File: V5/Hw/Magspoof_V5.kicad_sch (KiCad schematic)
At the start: 35 parts, among them J2 SWD, P1 USB_C_Plug_USB2.0, Q1 DMG3415U-7, SW1 ON, SW3 S1, SW4 SOURCE MAG, SW5 RESET, U1 CH552G, U2 AP2112K-3.3, U3 TC4424, U5 MCP73831

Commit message: feat(hw): components got reorganized
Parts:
- H1, H2, H3, H4: footprint MountingHole:MountingHole_2.2mm_M2 -> MountingHole:MountingHole_2.2mm_M2_DIN965_Pad

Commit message: feat(hw): TX and RX pins updated
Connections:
- net RXD: now also U1.8 (P3.0); no longer U1.4 (P1.6)
- net TXD: now also U1.7 (P3.1); no longer U1.5 (P1.7)
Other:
- moved on the sheet: C1, C2, U1

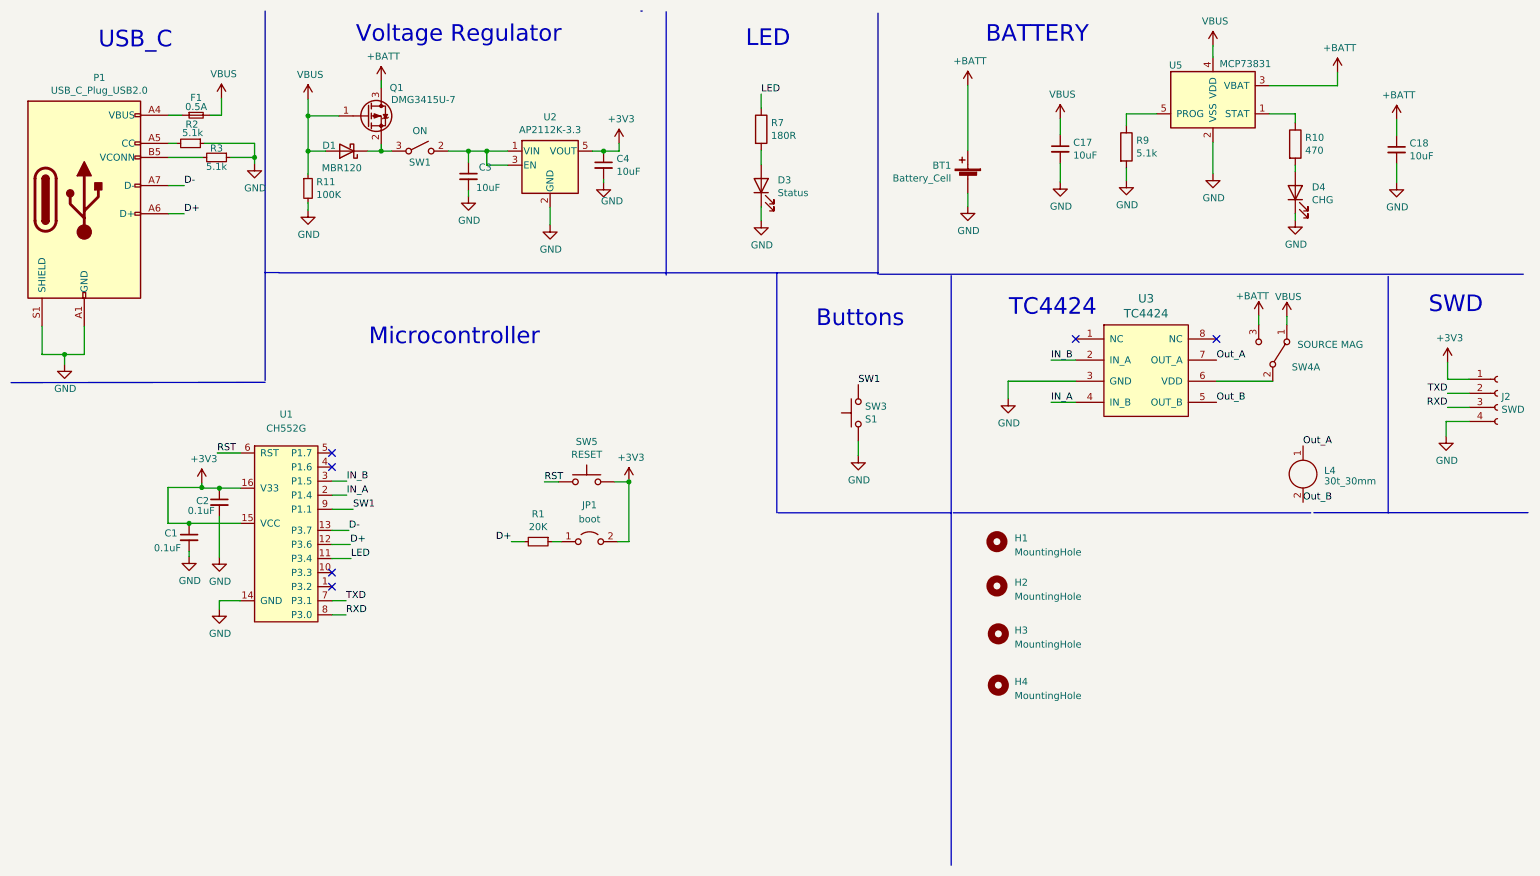
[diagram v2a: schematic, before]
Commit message: fix(hw): pins Serial boot
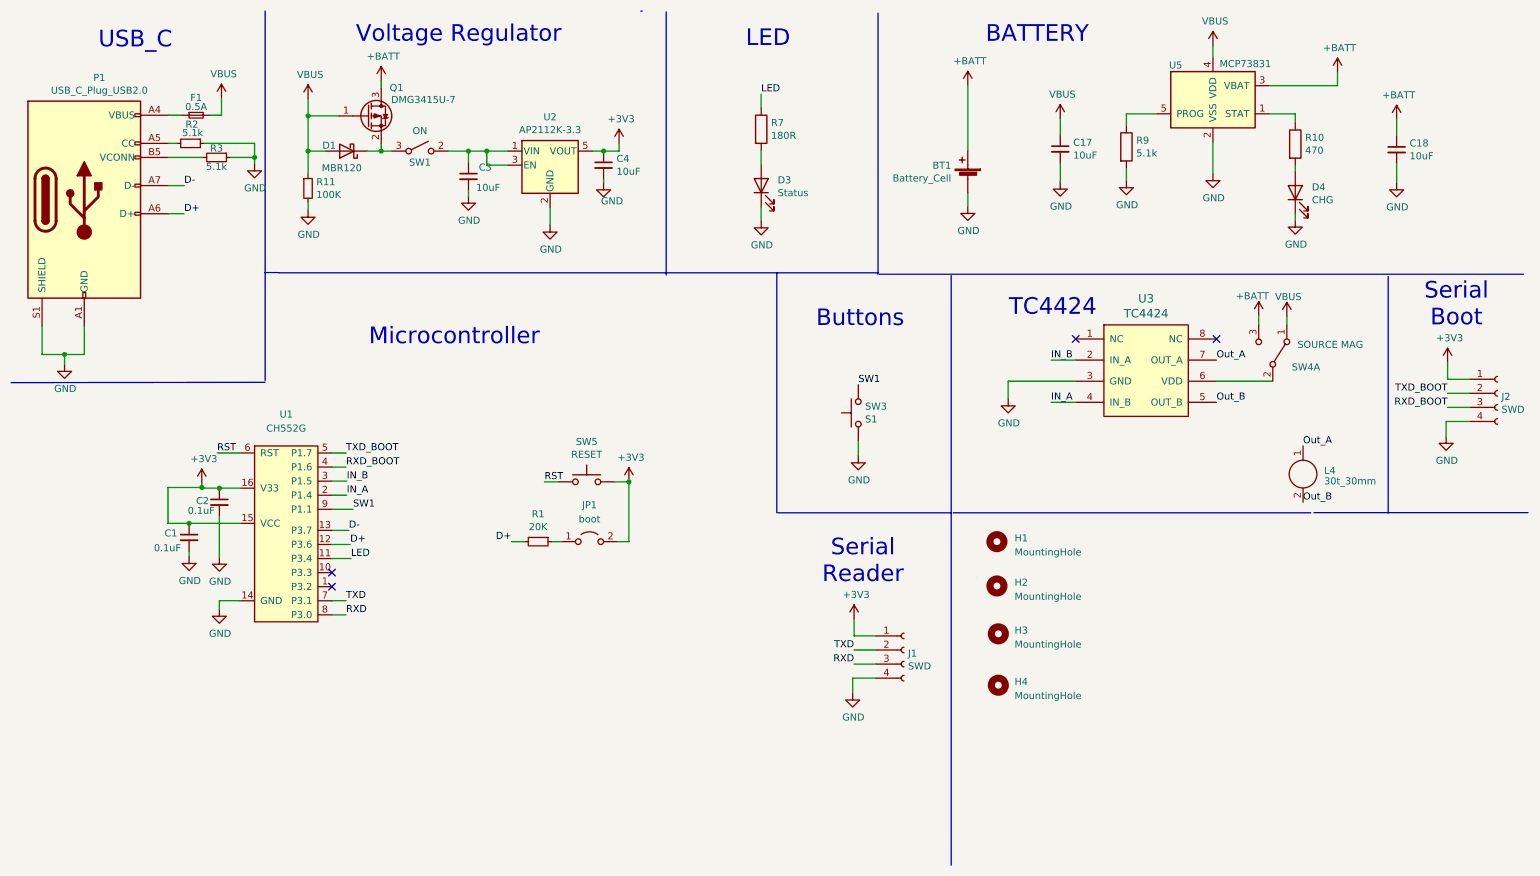
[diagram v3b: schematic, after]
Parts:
- added J1: SWD, Connector_PinHeader_2.54mm:PinHeader_1x04_P2.54mm_Vertical, symbol Connector:Conn_01x04_Female
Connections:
- net +3V3: now also J1.1 (Pin_1)
- net GND: now also J1.4 (Pin_4)
- net RXD: now also J1.3 (Pin_3); no longer J2.3 (Pin_3)
- net TXD: now also J1.2 (Pin_2); no longer J2.2 (Pin_2)
- net RXD_BOOT: now reaches U1.4 (P1.6)
- net RXD_BOOT: now also J2.3 (Pin_3)
- net TXD_BOOT: now reaches U1.5 (P1.7)
- net TXD_BOOT: now also J2.2 (Pin_2)
- no-connect marks 6 -> 4
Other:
- note added: "Serial Boot"
- note added: "Serial Reader"
- note removed: "SWD"

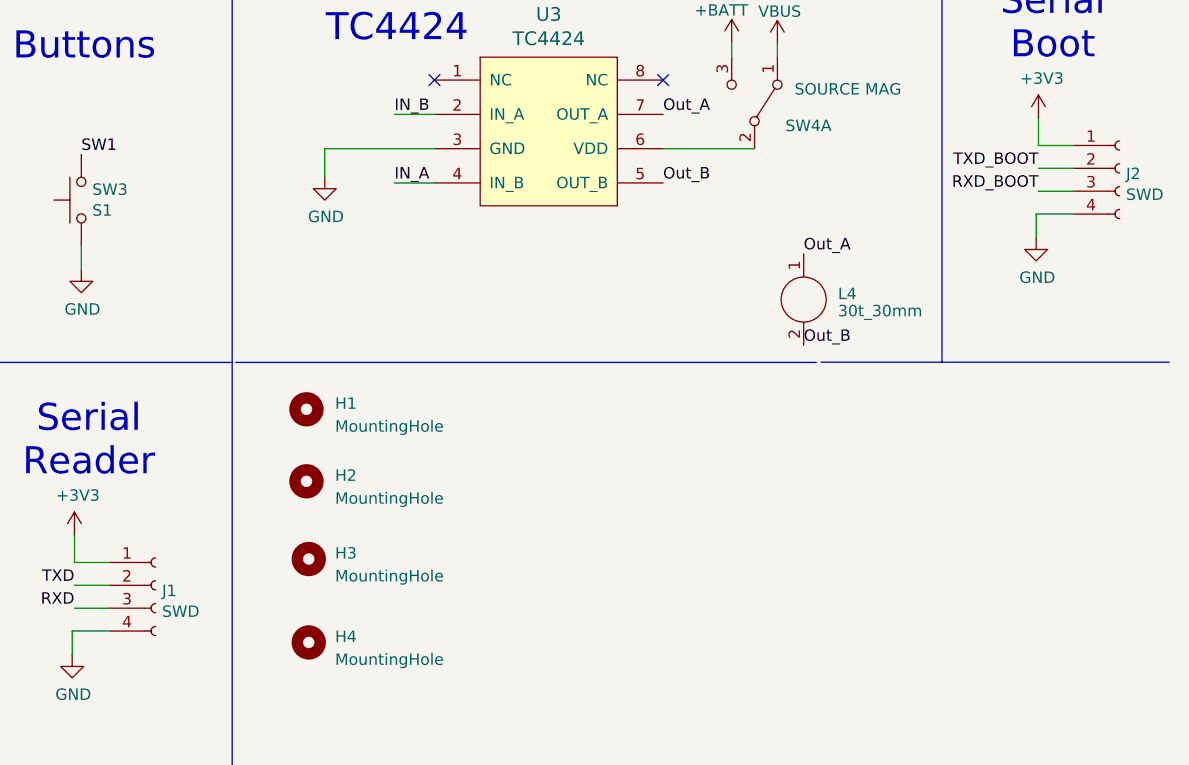
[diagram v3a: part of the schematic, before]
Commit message: feat(hw): added TX and RX Boot pins
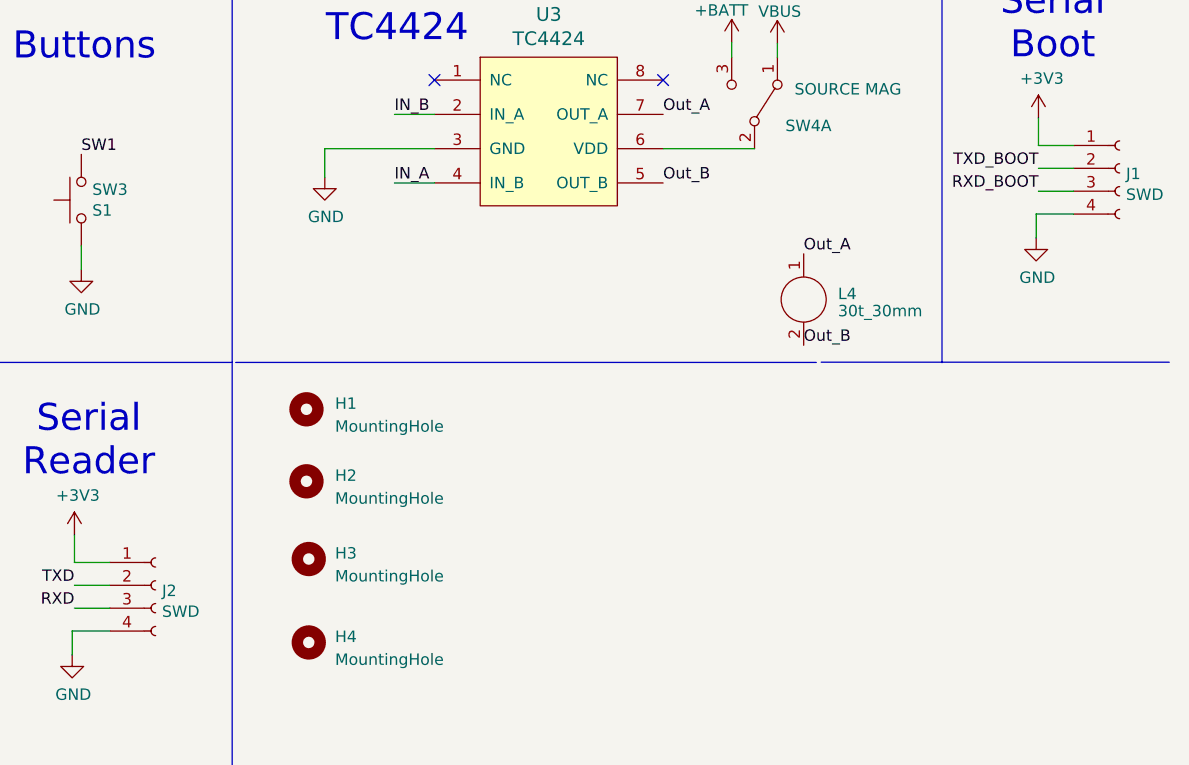
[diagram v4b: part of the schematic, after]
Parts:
- renumbered J2 to J1, J1 to J2
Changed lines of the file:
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@@
 		(on_board yes)
 		(dnp no)
-		(property "Reference" "J1"
+		(property "Reference" "J2"
 			(at 173.8122 127.6096 0)
 			(effects
@@
 			(project "Magspoof_V5"
 				(path "/a54f9b8d-da56-4b4b-9f0d-04fac56db24a"
-					(reference "J1")
+					(reference "J2")
 					(unit 1)
 				)
@@
 		(on_board yes)
 		(dnp no)
-		(property "Reference" "J2"
+		(property "Reference" "J1"
 			(at 280.924 81.28 0)
 			(effects
@@
 			(project "Magspoof_V5"
 				(path "/a54f9b8d-da56-4b4b-9f0d-04fac56db24a"
-					(reference "J2")
-					(unit 1)
-				)
+					(reference "J1")
+					(unit 1)
+				)

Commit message: feat(hw): BOM generated
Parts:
- J1: manf# - -> (none)
- J2: LCSC# (none) -> C6332197; manf# - -> HB-PH3-25414PB2GOP
- JP1: LCSC# (none) -> C492401; manf# (none) -> PZ254V-11-02P
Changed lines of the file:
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@@
 			)
 		)
-		(property "manf#" "-"
+		(property "manf#" "HB-PH3-25414PB2GOP "
 			(at -100.965 158.496 0)
+			(effects
+				(font
+					(size 1.27 1.27)
+				)
+				(hide yes)
+			)
+		)
+		(property "LCSC#" " C6332197"
+			(at 173.101 127 0)
 			(effects
 				(font
@@
 			)
 		)
+		(property "LCSC#" "C492401"
+			(at 116.332 107.442 0)
+			(effects
+				(font
+					(size 1.27 1.27)
+				)
+				(hide yes)
+			)
+		)
+		(property "manf#" "PZ254V-11-02P "
+			(at 116.332 107.442 0)
+			(effects
+				(font
+					(size 1.27 1.27)
+				)
+				(hide yes)
+			)
+		)
 		(pin "1"
 		)
@@
 			)
 		)
-		(property "manf#" "-"
+		(property "manf#" ""
 			(at 6.1468 112.1664 0)
 			(effects

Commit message: feat(hw): BOM got updated
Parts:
- BT1, H1, H2, H3, H4, J1, L4: now not fitted
- F1: LCSC# C136327 -> C2838887; manf# JFC0603-0500FS -> 0603FA-R500
- P1: LCSC# C2987386 -> (none); Proveedor LCSC -> MOUSER; manf# USB4105-GF-A -> 640-USB4105-GF-A
- R2, R3, R9: manf# HP02WAF2002TCE -> AR02BTC5101
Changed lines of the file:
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@@
 			)
 		)
-		(property "manf#" "HP02WAF2002TCE"
+		(property "manf#" " AR02BTC5101"
 			(at 49.022 38.1 0)
 			(effects
@@
 		(in_bom yes)
 		(on_board yes)
-		(dnp no)
+		(dnp yes)
 		(fields_autoplaced yes)
 		(property "Reference" "H1"
@@
 		(in_bom yes)
 		(on_board yes)
-		(dnp no)
+		(dnp yes)
 		(fields_autoplaced yes)
 		(property "Reference" "H2"
@@
 			)
 		)
-		(property "manf#" "HP02WAF2002TCE"
+		(property "manf#" " AR02BTC5101"
 			(at 44.323 35.56 0)
 			(effects
@@
 		(in_bom yes)
 		(on_board yes)
-		(dnp no)
+		(dnp yes)
 		(fields_autoplaced yes)
 		(property "Reference" "L4"
@@
 			)
 		)
-		(property "manf#" "HP02WAF2002TCE"
+		(property "manf#" " AR02BTC5101"
 			(at 213.233 36.195 0)
 			(effects
@@
 			)
 		)
-		(property "LCSC#" "C2987386"
+		(property "LCSC#" ""
 			(at 25.146 45.72 0)
 			(effects
@@
 			)
 		)
-		(property "manf#" "USB4105-GF-A"
+		(property "manf#" "640-USB4105-GF-A"
 			(at 25.146 45.72 0)
 			(effects
@@
 			)
 		)
-		(property "Proveedor" "LCSC"
+		(property "Proveedor" "MOUSER"
 			(at 25.146 45.72 0)
 			(effects
@@
 		(in_bom yes)
 		(on_board yes)
-		(dnp no)
+		(dnp yes)
 		(fields_autoplaced yes)
 		(property "Reference" "H3"
@@
 		(in_bom yes)
 		(on_board yes)
-		(dnp no)
+		(dnp yes)
 		(property "Reference" "BT1"
 			(at 181.61 39.5478 0)
@@
 		(in_bom yes)
 		(on_board yes)
-		(dnp no)
+		(dnp yes)
 		(fields_autoplaced yes)
 		(property "Reference" "H4"
@@
 		(in_bom yes)
 		(on_board yes)
-		(dnp no)
+		(dnp yes)
 		(property "Reference" "J1"
 			(at 280.924 81.28 0)
@@
 			)
 		)
-		(property "manf#" "JFC0603-0500FS"
+		(property "manf#" "0603FA-R500 "
 			(at 45.339 30.48 0)
 			(effects
@@
 			)
 		)
-		(property "LCSC#" "C136327"
+		(property "LCSC#" "C2838887"
 			(at 45.339 30.48 0)
 			(effects

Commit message: feat(hw): USB manufacture part updated
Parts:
- J2, JP1: Proveedor (none) -> LCSC
- P1: LCSC# (none) -> C393939; Proveedor MOUSER -> LCSC; manf# 640-USB4105-GF-A -> TYPE-C16PIN
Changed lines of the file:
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@@
 			)
 		)
-		(property "LCSC#" ""
+		(property "LCSC#" "C393939"
 			(at 25.146 45.72 0)
 			(effects
@@
 			)
 		)
-		(property "manf#" "640-USB4105-GF-A"
+		(property "manf#" " TYPE-C16PIN"
 			(at 25.146 45.72 0)
 			(effects
@@
 			)
 		)
-		(property "Proveedor" "MOUSER"
+		(property "Proveedor" "LCSC"
 			(at 25.146 45.72 0)
 			(effects
@@
 			)
 		)
+		(property "Proveedor" "LCSC"
+			(at 173.101 127 0)
+			(effects
+				(font
+					(size 1.27 1.27)
+				)
+				(hide yes)
+			)
+		)
 		(pin "1"
 		)
@@
 			(at 116.332 107.442 0)
 			(effects
+				(font
+					(size 1.27 1.27)
+				)
+				(hide yes)
+			)
+		)
+		(property "Proveedor" "LCSC"
+			(at 116.332 107.442 0)
+			(effects

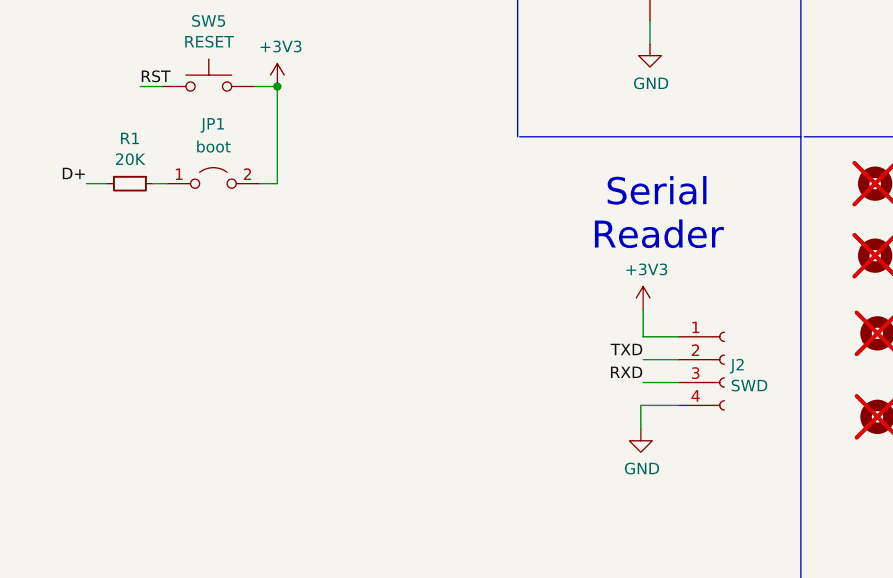
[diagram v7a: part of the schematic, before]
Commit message: fix(hw): DNP update of the list components
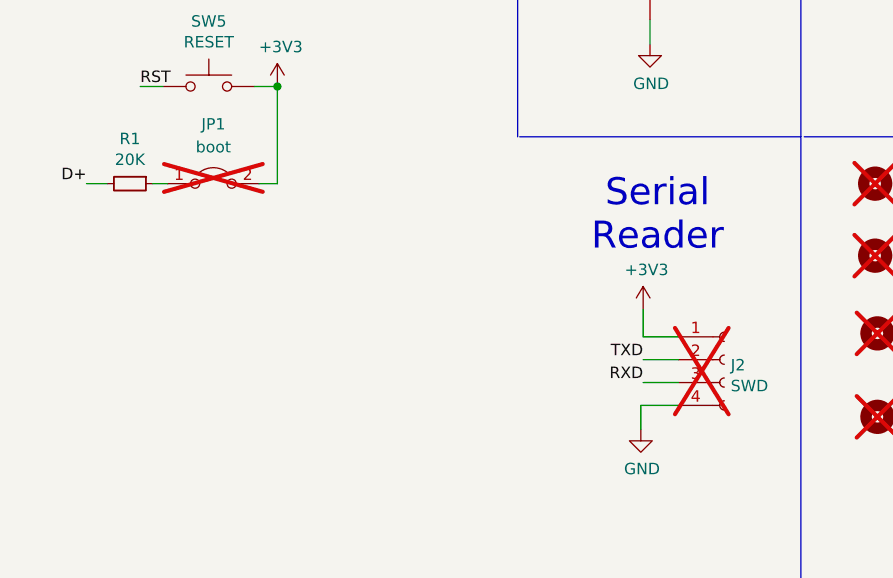
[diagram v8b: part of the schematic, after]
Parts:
- J2, JP1: now not fitted
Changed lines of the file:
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@@
 		(in_bom yes)
 		(on_board yes)
-		(dnp no)
+		(dnp yes)
 		(property "Reference" "J2"
 			(at 173.8122 127.6096 0)
@@
 		(in_bom yes)
 		(on_board yes)
-		(dnp no)
+		(dnp yes)
 		(fields_autoplaced yes)
 		(property "Reference" "JP1"
